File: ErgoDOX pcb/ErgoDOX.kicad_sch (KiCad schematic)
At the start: 83 parts, among them J1 USB, J10 USB VCC, J2 3.5mm, J3 JMP, J4 JMP, J5 BT_JMP, J6 EN_JMP, J7 PROG, J8 JTAG, J9 USB GND, SW0:10 SW0:3, SW0:11 SW0:2, SW0:12 SW0:1, SW0:7 SW0:6, SW0:8 SW0:5, SW0:9 SW0:4, SW1:10 SW1:3, SW1:11 SW1:2, SW1:12 SW1:1, SW1:13 SW1:0, SW1:9 SW1:4, SW2:10 SW2:3, SW2:11 SW2:2, SW2:12 SW2:1, SW2:13 SW2:0, SW2:7 SW2:6, SW2:8 SW2:5, SW2:9 SW2:4, SW3:10 SW3:3, SW3:11 SW3:2, SW3:12 SW3:1, SW3:13 SW3:0, SW3:8 SW3:5, SW3:9 SW3:4, SW4:10 SW4:3, SW4:11 SW4:2, SW4:12 SW4:1, SW4:13 SW4:0, SW4:7 SW4:6, SW4:8 SW4:5, SW4:9 SW4:4, SW5:10 SW5:3, SW5:11 SW5:2, SW5:12 SW5:1, SW5:13 SW5:0, SW5:7 SW5:6, SW5:8 SW5:5, SW5:9 SW5:4, U1 LM337_SOT223

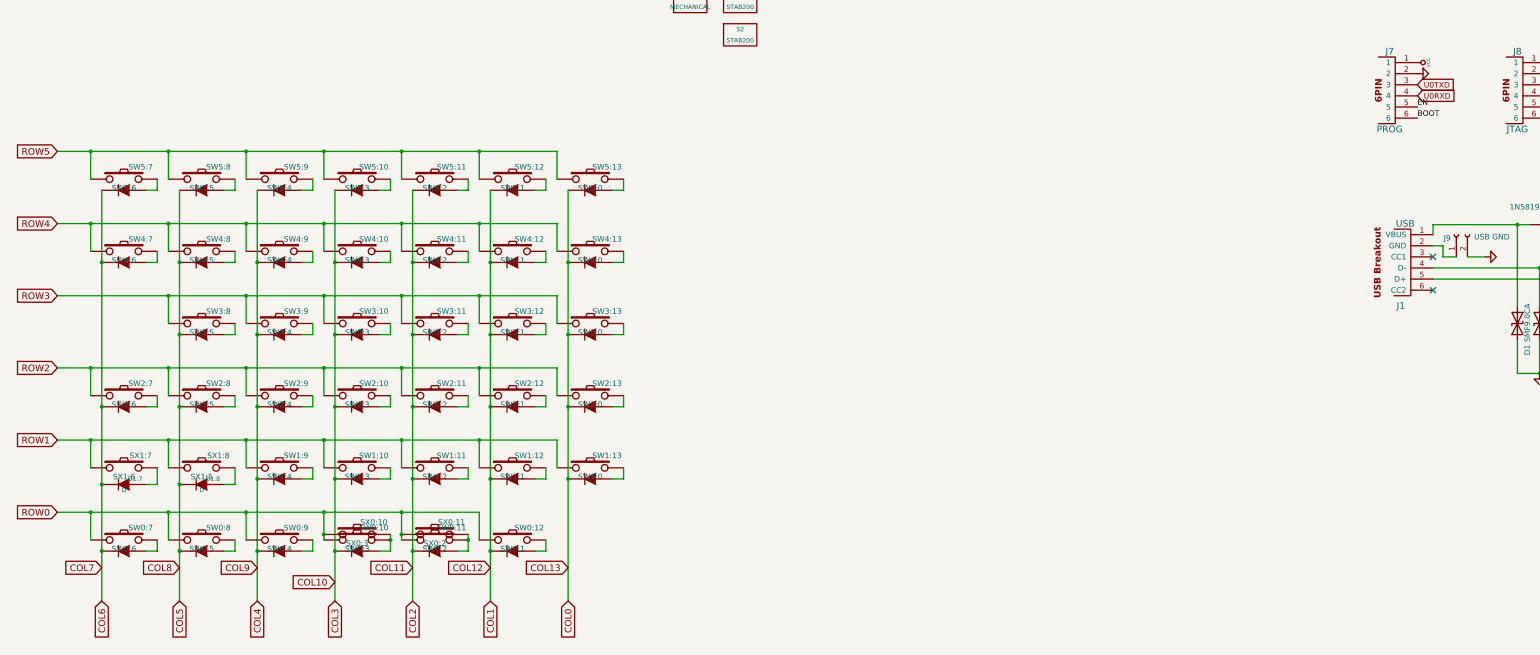
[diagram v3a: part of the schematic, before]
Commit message: First route of board
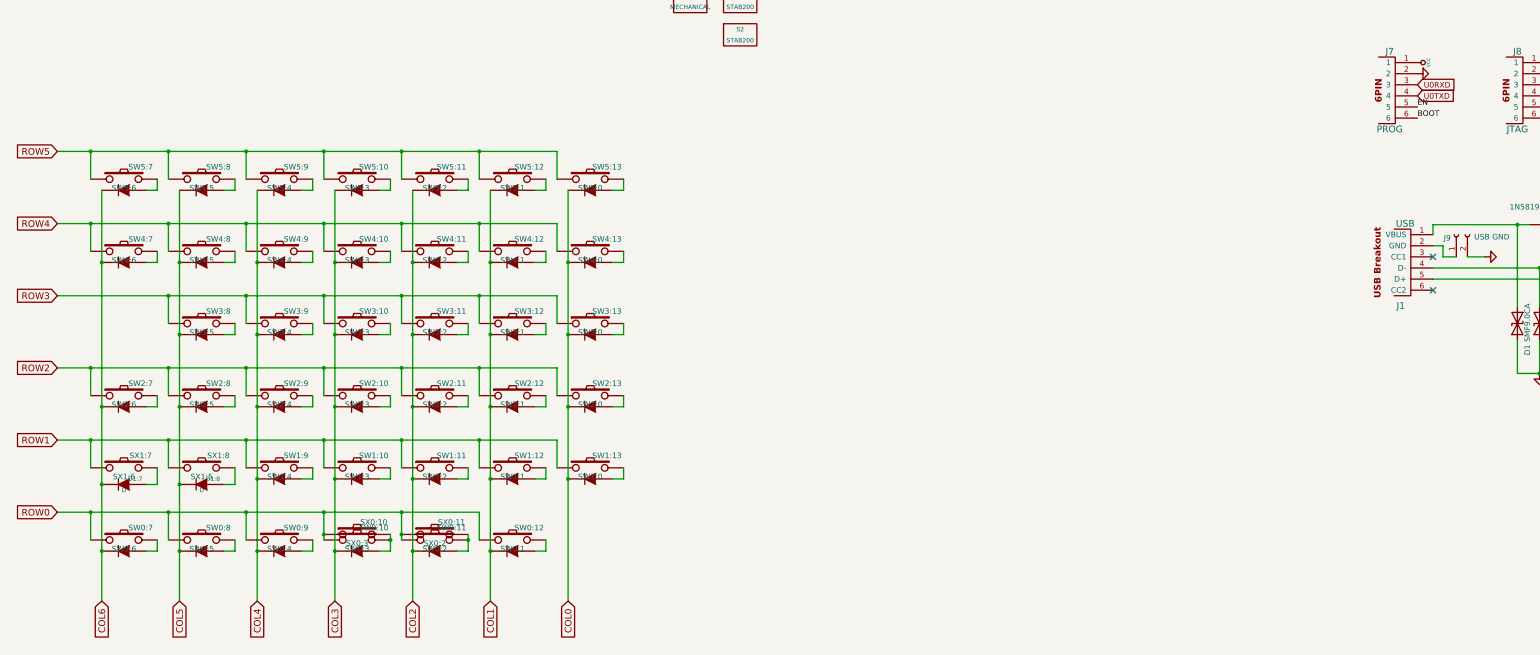
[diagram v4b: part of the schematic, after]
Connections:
- net U0RXD: now also J7.3; no longer J7.4
- net U0TXD: now also J7.4; no longer J7.3
- net COL10 renamed COL3
- net COL11 renamed COL2
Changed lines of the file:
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@@
     (effects (font (size 1.27 1.27)) (justify left bottom))
-  )
-  (global_label "COL10" (shape input) (at 96.52 245.872 180) (fields_autoplaced)
-    (effects (font (size 1.524 1.524)) (justify right))
-    (property "Intersheet References" "${INTERSHEET_REFS}" (id 0) (at 86.474 245.7768 0)
-      (effects (font (size 1.524 1.524)) (justify right) hide)
-    )
   )
   (global_label "COL1" (shape input) (at 132.08 250.19 270) (fields_autoplaced)
@@
     (property "Intersheet References" "${INTERSHEET_REFS}" (id 0) (at 131.9848 258.7846 90)
       (effects (font (size 1.524 1.524)) (justify right) hide)
-    )
-  )
-  (global_label "U0RXD" (shape input) (at 344.17 134.62 0) (fields_autoplaced)
-    (effects (font (size 1.27 1.27)) (justify left))
-    (property "Intersheet References" "${INTERSHEET_REFS}" (id 0) (at 352.7837 134.5406 0)
-      (effects (font (size 1.27 1.27)) (justify left) hide)
     )
   )
@@
     (effects (font (size 1.524 1.524)) (justify right))
     (property "Intersheet References" "${INTERSHEET_REFS}" (id 0) (at 60.8648 258.7846 90)
-      (effects (font (size 1.524 1.524)) (justify right) hide)
-    )
-  )
-  (global_label "COL13" (shape input) (at 149.86 242.57 180) (fields_autoplaced)
-    (effects (font (size 1.524 1.524)) (justify right))
-    (property "Intersheet References" "${INTERSHEET_REFS}" (id 0) (at 139.814 242.4748 0)
       (effects (font (size 1.524 1.524)) (justify right) hide)
     )
@@
     )
   )
-  (global_label "COL8" (shape input) (at 60.96 242.57 180) (fields_autoplaced)
-    (effects (font (size 1.524 1.524)) (justify right))
-    (property "Intersheet References" "${INTERSHEET_REFS}" (id 0) (at 52.3654 242.6652 0)
-      (effects (font (size 1.524 1.524)) (justify right) hide)
-    )
-  )
   (global_label "VCC_5V" (shape input) (at 388.62 164.084 90) (fields_autoplaced)
     (effects (font (size 1.27 1.27)) (justify left))
@@
     )
   )
+  (global_label "U0RXD" (shape input) (at 344.17 132.08 0) (fields_autoplaced)
+    (effects (font (size 1.27 1.27)) (justify left))
+    (property "Intersheet References" "${INTERSHEET_REFS}" (id 0) (at 352.7837 132.0006 0)
+      (effects (font (size 1.27 1.27)) (justify left) hide)
+    )
+  )
   (global_label "D-" (shape input) (at 392.43 173.99 0) (fields_autoplaced)
     (effects (font (size 1.27 1.27)) (justify left))
     (property "Intersheet References" "${INTERSHEET_REFS}" (id 0) (at 397.5966 173.9106 0)
       (effects (font (size 1.27 1.27)) (justify left) hide)
-    )
-  )
-  (global_label "COL7" (shape input) (at 43.18 242.57 180) (fields_autoplaced)
-    (effects (font (size 1.524 1.524)) (justify right))
-    (property "Intersheet References" "${INTERSHEET_REFS}" (id 0) (at 34.5854 242.6652 0)
-      (effects (font (size 1.524 1.524)) (justify right) hide)
     )
   )
@@
     (property "Intersheet References" "${INTERSHEET_REFS}" (id 0) (at 379.2118 139.6206 0)
       (effects (font (size 1.27 1.27)) (justify left) hide)
-    )
-  )
-  (global_label "U0TXD" (shape input) (at 344.17 132.08 0) (fields_autoplaced)
-    (effects (font (size 1.27 1.27)) (justify left))
-    (property "Intersheet References" "${INTERSHEET_REFS}" (id 0) (at 352.4813 132.0006 0)
-      (effects (font (size 1.27 1.27)) (justify left) hide)
-    )
-  )
-  (global_label "COL11" (shape input) (at 114.3 242.57 180) (fields_autoplaced)
-    (effects (font (size 1.524 1.524)) (justify right))
-    (property "Intersheet References" "${INTERSHEET_REFS}" (id 0) (at 104.254 242.6652 0)
-      (effects (font (size 1.524 1.524)) (justify right) hide)
     )
   )
@@
     )
   )
-  (global_label "COL9" (shape input) (at 78.74 242.57 180) (fields_autoplaced)
-    (effects (font (size 1.524 1.524)) (justify right))
-    (property "Intersheet References" "${INTERSHEET_REFS}" (id 0) (at 70.1454 242.6652 0)
-      (effects (font (size 1.524 1.524)) (justify right) hide)
-    )
-  )
   (global_label "ROW3" (shape input) (at 33.02 180.34 180) (fields_autoplaced)
     (effects (font (size 1.524 1.524)) (justify right))
@@
     )
   )
-  (global_label "COL12" (shape input) (at 132.08 242.57 180) (fields_autoplaced)
-    (effects (font (size 1.524 1.524)) (justify right))
-    (property "Intersheet References" "${INTERSHEET_REFS}" (id 0) (at 122.034 242.4748 0)
-      (effects (font (size 1.524 1.524)) (justify right) hide)
+  (global_label "U0TXD" (shape input) (at 344.17 134.62 0) (fields_autoplaced)
+    (effects (font (size 1.27 1.27)) (justify left))
+    (property "Intersheet References" "${INTERSHEET_REFS}" (id 0) (at 352.4813 134.5406 0)
+      (effects (font (size 1.27 1.27)) (justify left) hide)
     )
   )

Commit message: Add back components, silk screen
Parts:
- added D? (x3): SMF9.0CA, Diode_SMD:D_SOD-123, symbol Diode:ESD9B3.3ST5G
- added D?: 1N5819HW-7-F, Diode_SMD:D_SOD-123, symbol Diode:1N5819
- added J?: USB_LH, ErgoDOX pcb:SF USB-C Breakout, symbol component:6PIN
- added SW_RST?: RST_LH, Button_Switch_SMD:SW_SPST_B3U-1000P, symbol component:SWITCH_PUSH
- added SW_RST?: BOOT_LH, Button_Switch_SMD:SW_SPST_B3U-1000P, symbol component:SWITCH_PUSH
- added U?: LM337_SOT223, Package_TO_SOT_SMD:SOT-223-3_TabPin2, symbol Regulator_Linear:LM337_SOT223
- J1: value USB -> USB_RH
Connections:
- net D+: now also D?.2 (A2), J?.5 (D+)
- net D-: now also D?.2 (A2), J?.4 (D-)
- net GND: now also D?.1 (A1), D?.1 (A1), D?.1 (A1), SW_RST?.0 (GND), SW_RST?.0 (GND), SW_RST?.2, SW_RST?.2, U?.1 (ADJ)
- net VCC: now also U?.3 (VO)
- net VCC_5V: now also U?.2 (VI)
- net VBUS: now reaches D1.2 (A2), D3.2 (A), J1.1 (VBUS)
- net VBUS: now also D?.2 (A), D?.2 (A2), J?.1 (VBUS)
- net USB_VCC: now reaches D3.1 (K), J10.1 (Pin_1)
- net USB_VCC: now also D?.1 (K)
- net GBUS: now reaches J1.2 (GND), J9.1 (Pin_1)
- net GBUS: now also J?.2 (GND)
- net BT_JUMP: now reaches C5.2, J5.1 (Pin_1), SW_RST2.1
- net BT_JUMP: now also SW_RST?.1
- net EN_JMP: now reaches C4.2, J6.1 (Pin_1), SW_RST1.1
- net EN_JMP: now also SW_RST?.1
- no-connect marks 2 -> 4
